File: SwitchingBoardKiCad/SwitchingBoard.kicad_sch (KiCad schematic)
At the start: 62 parts, among them J1 Screw_Terminal_01x02, J2 Screw_Terminal_01x02, J3 Screw_Terminal_01x02, J4 Screw_Terminal_01x02, J5 Screw_Terminal_01x02, J6 Screw_Terminal_01x03, J7 Screw_Terminal_01x02, J8 Screw_Terminal_01x02, J9 Screw_Terminal_01x02, K1 FINDER-30.22, Q1 Q_TRIAC_A2GA1, Q2 BTB16-800CW, Q3 BTB16-800CW

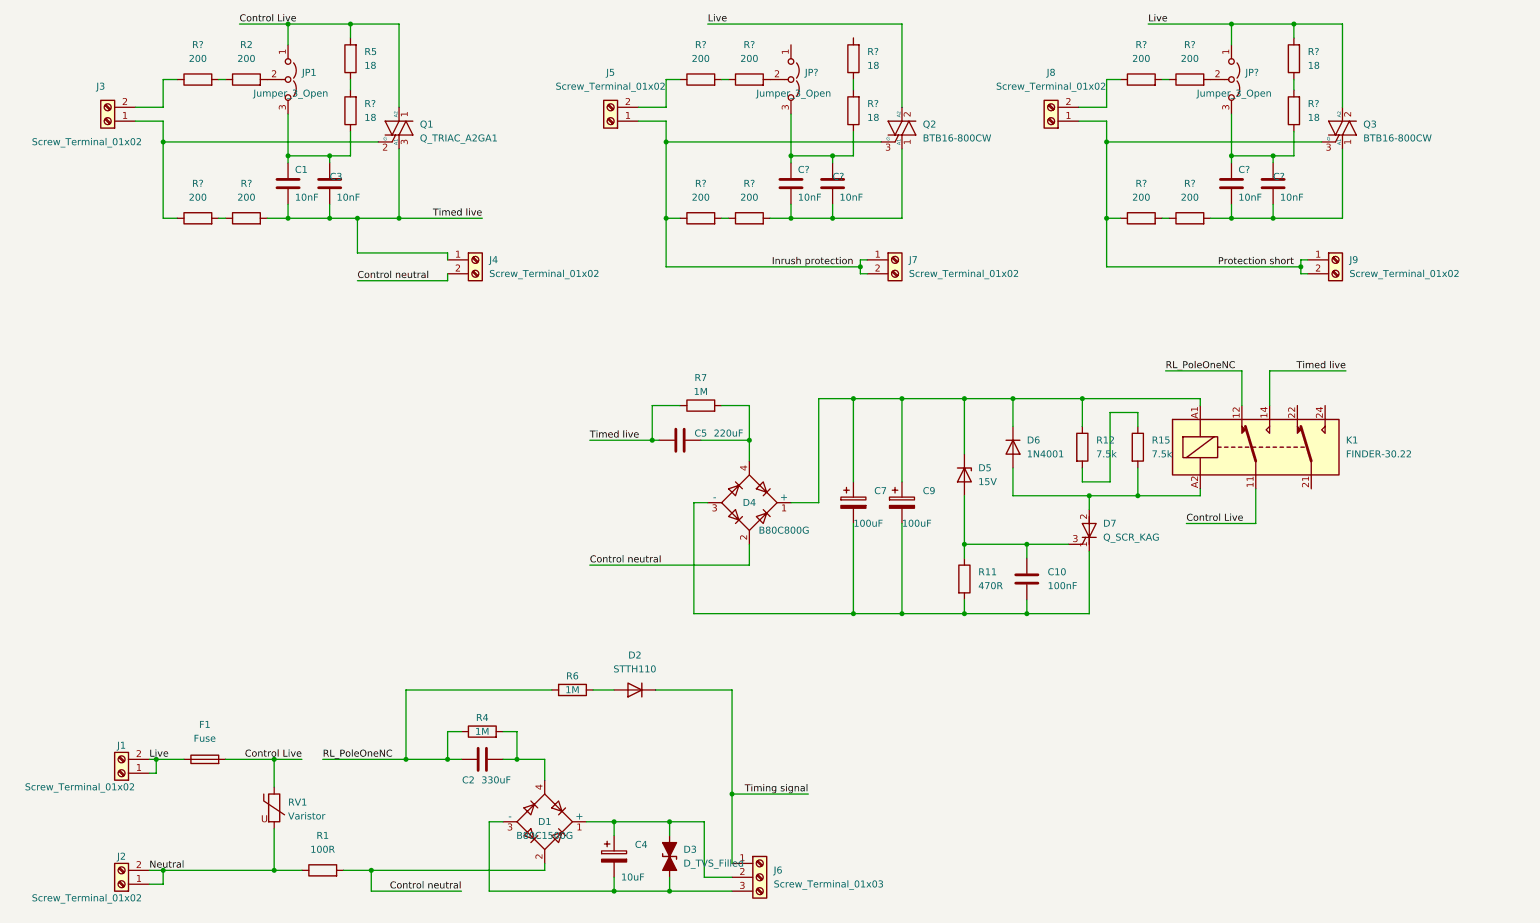
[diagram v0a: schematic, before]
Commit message: Fixed schematic connections.
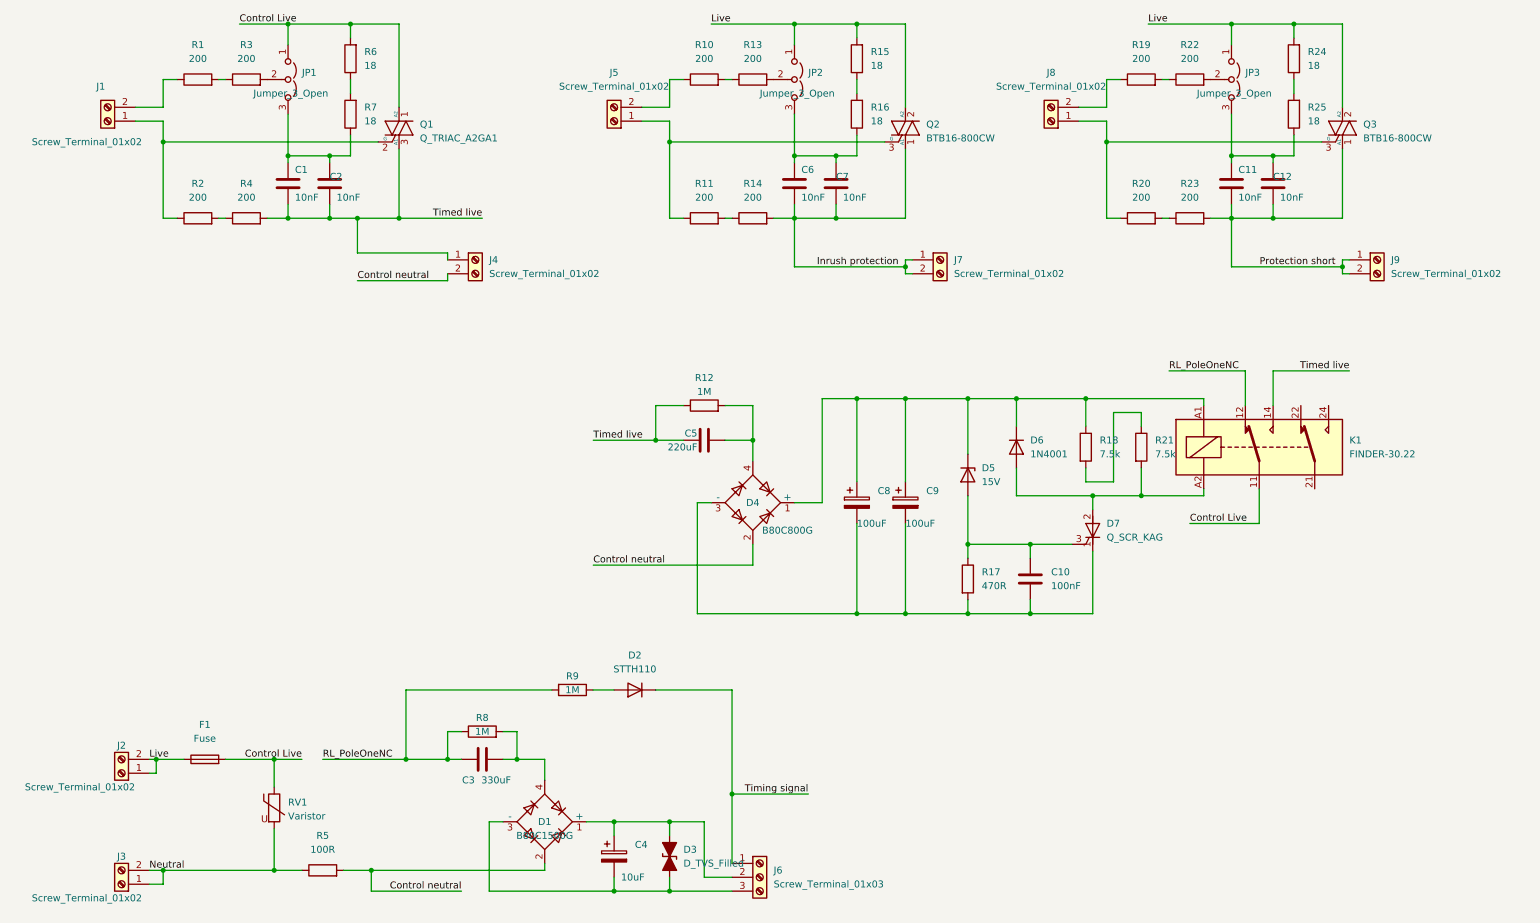
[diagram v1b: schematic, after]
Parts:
- gave numbers to parts that had none: 22
- renumbered C3 to C2, C2 to C3, C7 to C8, J3 to J1, J1 to J2, J2 to J3, R7 to R12, R11 to R17, R12 to R18, R15 to R21, R2 to R3, R1 to R5, R5 to R6, R4 to R8, R6 to R9
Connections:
- net Inrush protection: now also C6.1, C7.1, Q2.1 (A1), R14.2; no longer J5.1 (Pin_1), Q2.3 (G), R11.1
- net Live: now also JP2.1 (A), R15.2
- net Protection short: now also C11.1, C12.1, Q3.1 (A1), R23.2; no longer J8.1 (Pin_1), Q3.3 (G), R20.1
- new net: J8.1 (Pin_1), Q3.3 (G), R20.1
- new net: J5.1 (Pin_1), Q2.3 (G), R11.1
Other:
- moved on the sheet: C10, C5, C6, C7, C8, C9, D4, D5, D6, D7, J5, J7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

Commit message: Layout changes.
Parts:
- D3: value D_TVS_Filled -> P6KE68A
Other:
- moved on the sheet: C3, C4, D1, D2, D3, R5, R8, R9
